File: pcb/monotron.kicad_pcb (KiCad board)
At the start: 2 copper layers, 133.3 x 94 mm, 51 parts, among them J1 Mono / Stereo, J10 DIN5-180, J11 DIN5-180, J12 DE9M, J13 DB25_Female, J14 Mini-DIN-6, J15 Mini-DIN-6, J2 Jack-DC, J3 1x7 Header, J4 AudioJack3, J5 DE9F, J6 1x4 Header, J7 DE15HD, J8 2x6 Header, J9 DIN5-180, U1 TM4C123G_Launchpad, U2 MAX3232, U3 74LS14, U4 6N138, U5 ATmega48A-PU

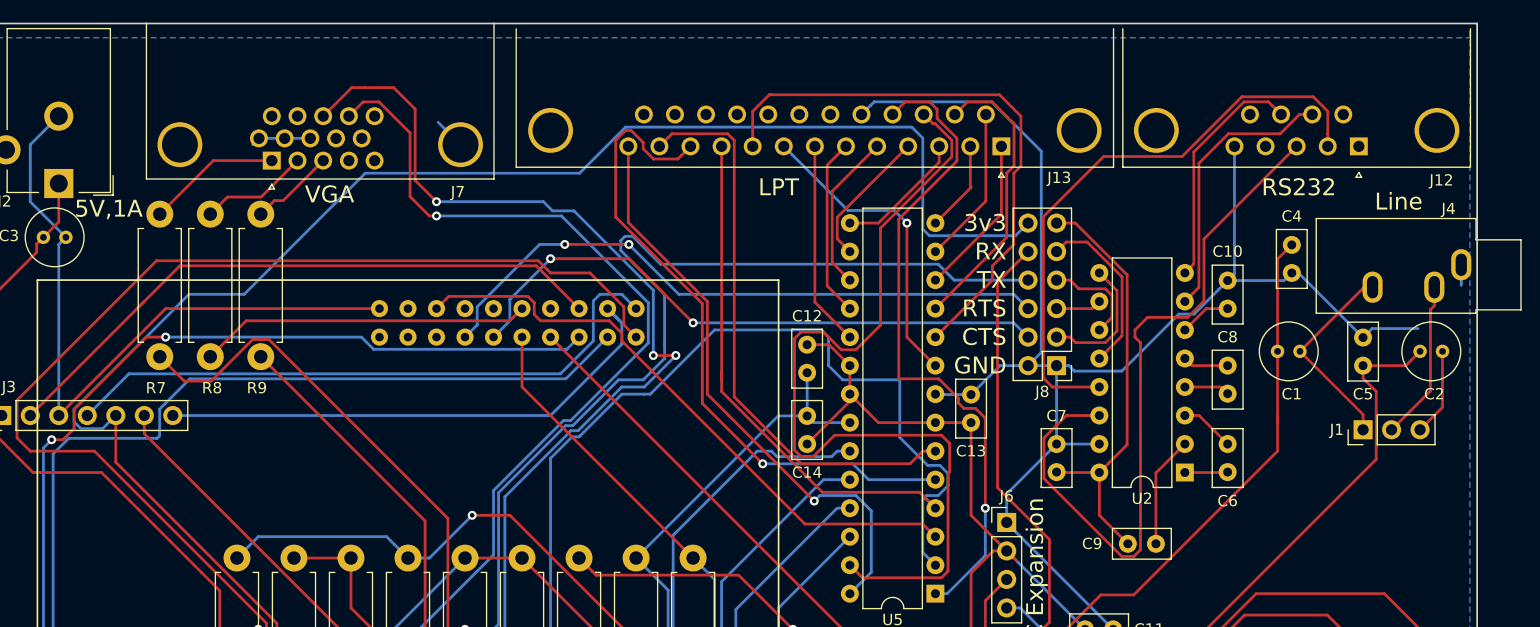
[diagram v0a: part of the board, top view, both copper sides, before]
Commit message: Fix split ground-plane. Moved a few bottom tracks to make ground fill larger.
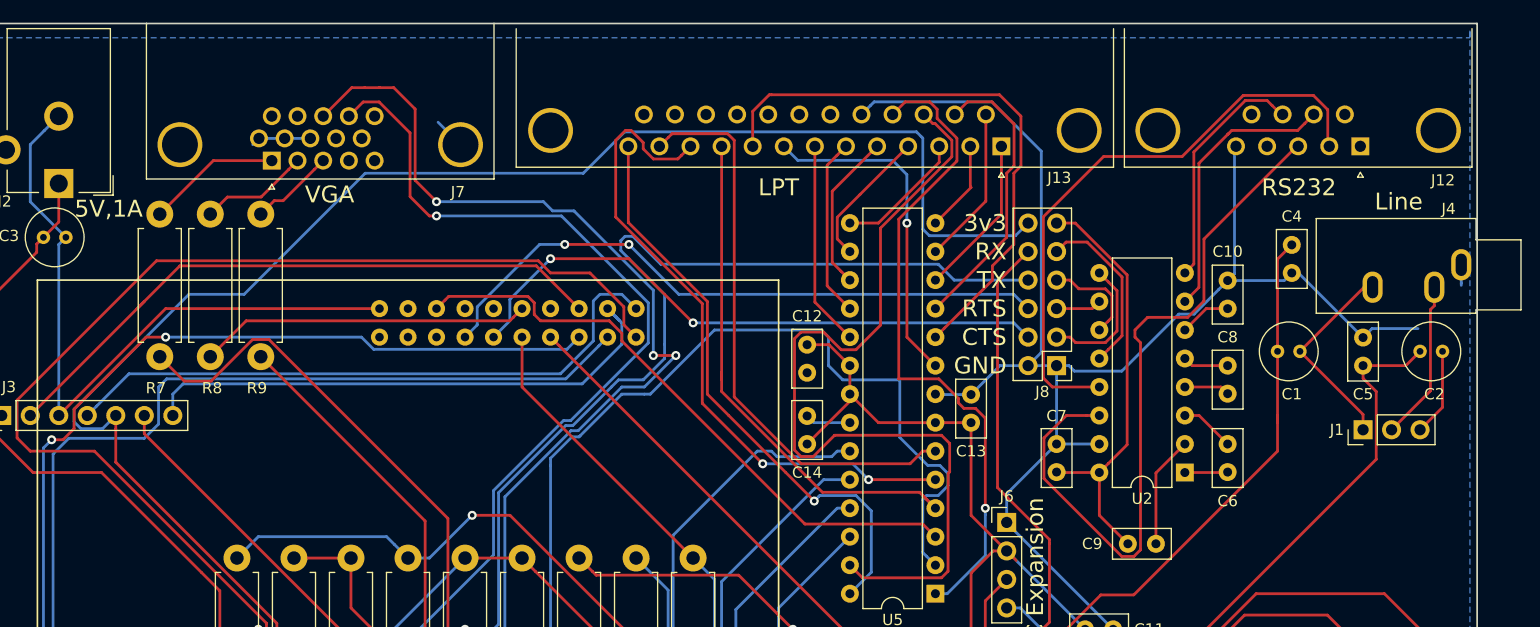
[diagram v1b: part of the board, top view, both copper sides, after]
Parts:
- moved J12 0.14 mm to (196.6, 46.5)
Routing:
- net GND: track 400.8 -> 376.5 mm
- net /Monotron I/O Expansion/D6: track 27.6 -> 30.1 mm
- net /PA3_SD_CS: track 47.9 -> 49.0 mm
- net /Monotron I/O Expansion/BUSY: vias 1 -> 2

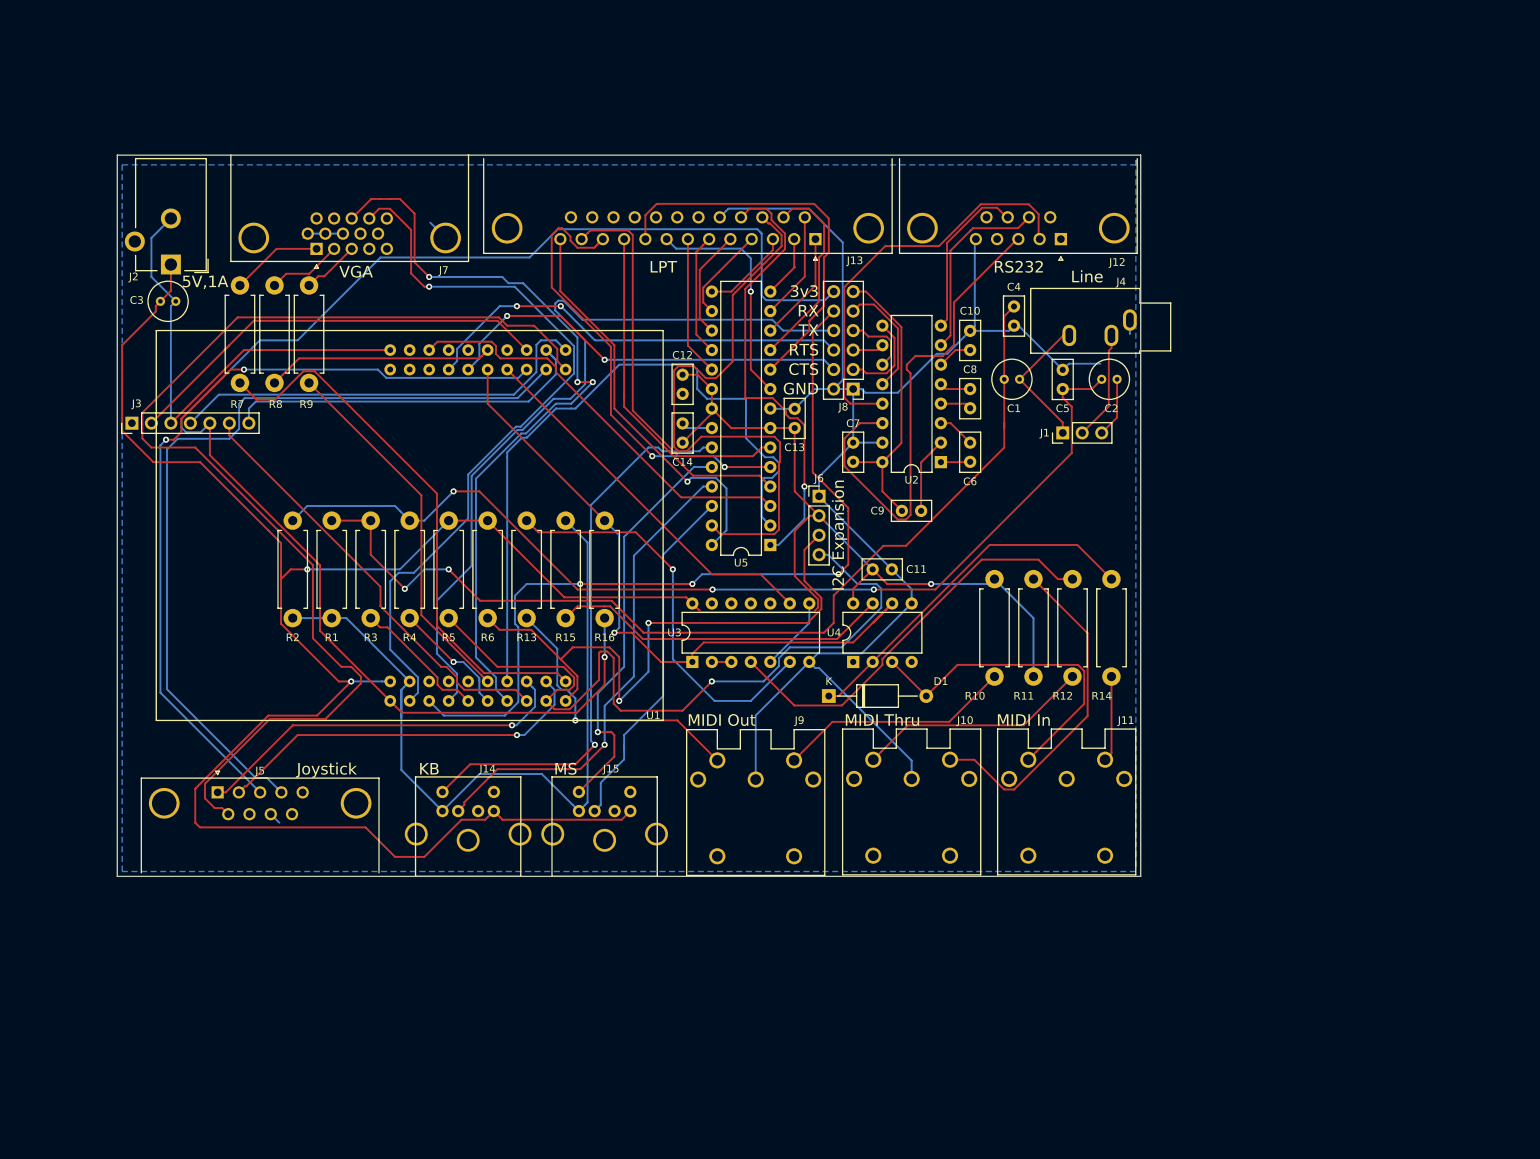
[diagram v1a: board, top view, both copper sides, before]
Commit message: Finished adding RTC to PCB layout.
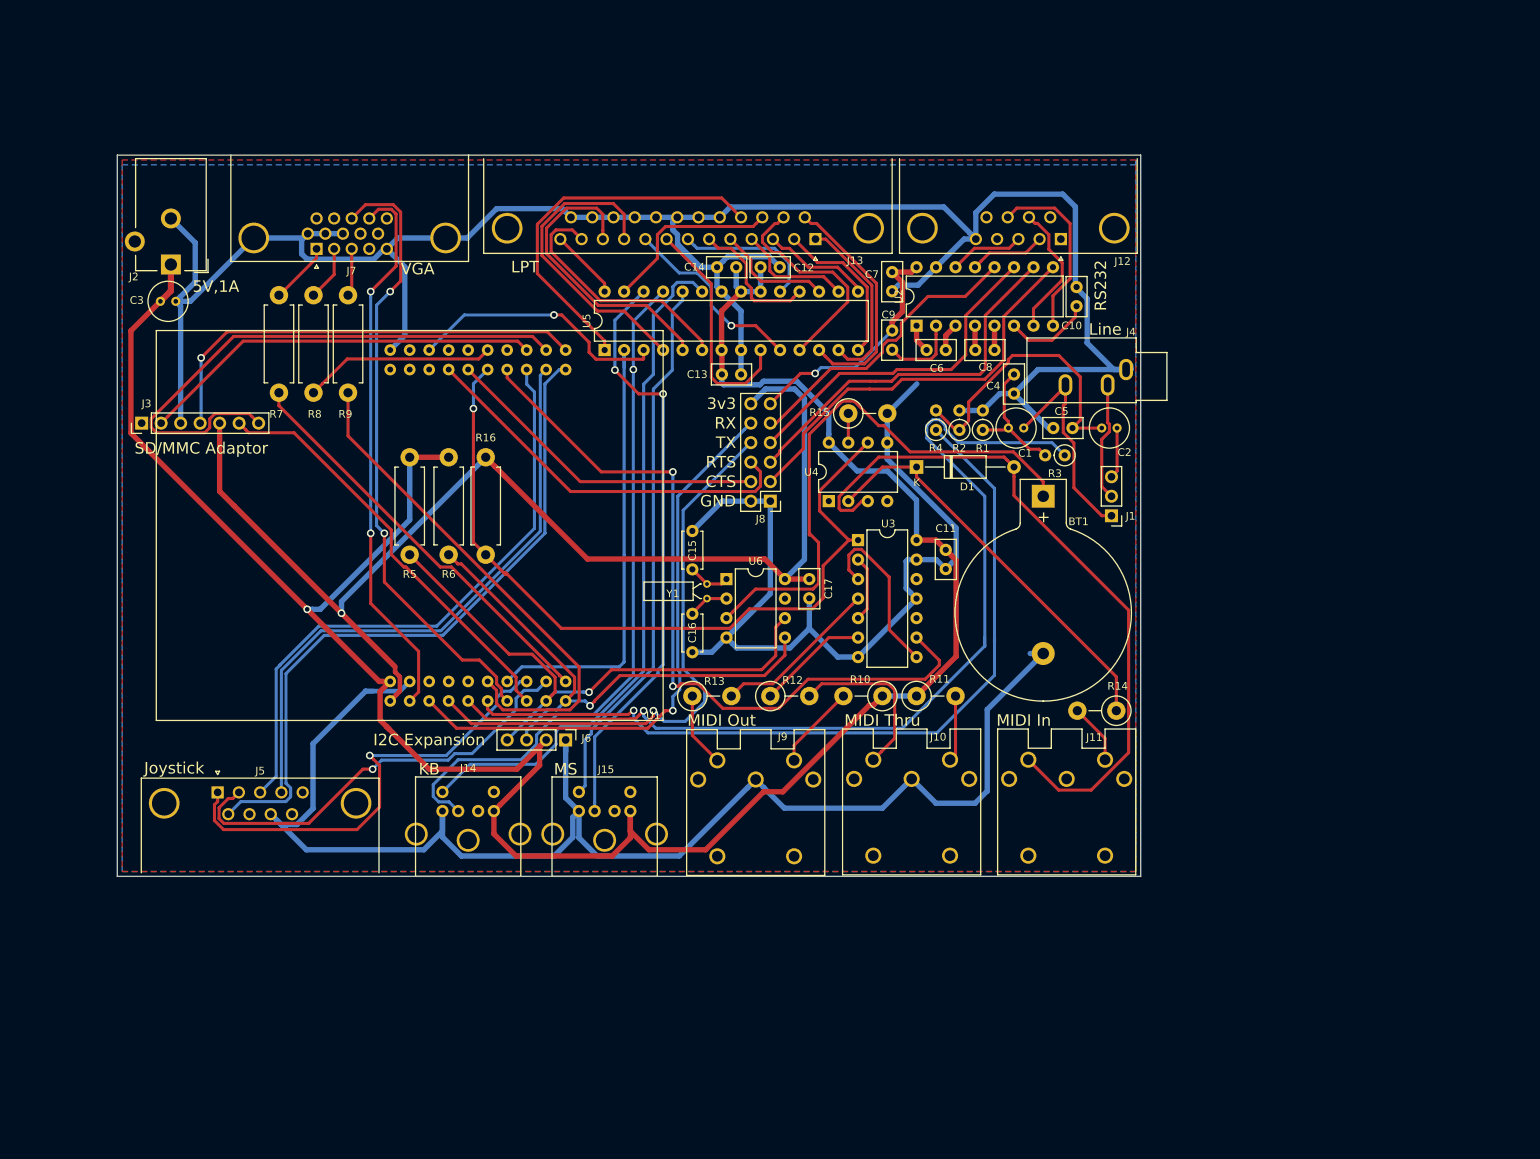
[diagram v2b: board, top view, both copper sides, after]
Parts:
- added BT1: Battery, Battery:BatteryHolder_Keystone_103_1x20mm, F.Cu at (194.3, 80.0)
- added C15: 12p, Capacitor_THT:C_Disc_D4.7mm_W2.5mm_P5.00mm, F.Cu at (148.6, 84.5)
- added C16: 12p, Capacitor_THT:C_Disc_D4.7mm_W2.5mm_P5.00mm, F.Cu at (148.6, 100.3)
- added C17: 100n, Capacitor_THT:C_Disc_D5.0mm_W2.5mm_P2.50mm, F.Cu at (163.8, 90.8)
- added U6: MCP7940N-xP, Package_DIP:DIP-8_W7.62mm, F.Cu at (153.0, 90.8)
- added Y1: 32,768 kHz, Crystal:Crystal_DS26_D2.0mm_L6.0mm_Horizontal, F.Cu at (150.5, 91.4)
- R1, R2, R3, R4: footprint Resistor_THT:R_Axial_DIN0411_L9.9mm_D3.6mm_P12.70mm_Horizontal -> Resistor_THT:R_Axial_DIN0207_L6.3mm_D2.5mm_P2.54mm_Vertical
- R10, R11, R12, R13, R14, R15: footprint Resistor_THT:R_Axial_DIN0411_L9.9mm_D3.6mm_P12.70mm_Horizontal -> Resistor_THT:R_Axial_DIN0411_L9.9mm_D3.6mm_P5.08mm_Vertical
- moved R3 92.9 mm to (197.1, 74.7), turned to 180 degrees
- moved R2 87.7 mm to (183.4, 71.4), turned to 90 degrees
- moved R1 85.7 mm to (186.4, 71.4), turned to 90 degrees
- moved R4 72.8 mm to (180.3, 71.4)
- moved J6 45.8 mm to (132.1, 111.8), turned to 270 degrees
- moved R15 45.5 mm to (168.9, 69.2), turned to 0 degrees
- moved R12 42.2 mm to (158.8, 106.0), turned to 0 degrees
- moved U5 33.3 mm to (137.2, 61.0), turned to 90 degrees
- moved D1 32.0 mm to (177.8, 76.2)
- moved U3 26.8 mm to (170.2, 85.7), turned to 0 degrees
- moved R16 26.1 mm to (121.7, 74.9), turned to 270 degrees
- moved C7 25.2 mm to (174.6, 50.8), turned to 270 degrees
- moved C14 23.9 mm to (154.3, 50.2), turned to 180 degrees
- moved R13 23.9 mm to (148.6, 106.0), turned to 0 degrees
- moved C9 23.5 mm to (174.6, 58.4), turned to 270 degrees
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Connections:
- U3 pad 3: Net-(U3-Pad2) -> Net-(U3-Pad3)
- U3 pad 4: Net-(R12-Pad1) -> Net-(R13-Pad2)
- U3 pad 5: Net-(U3-Pad5) -> Net-(U3-Pad2)
- U3 pad 6: Net-(R13-Pad2) -> Net-(R12-Pad1)
- U3 pad 8: Net-(U3-Pad5) -> Net-(U3-Pad3)
- U5 pad 12: /Monotron I/O Expansion/STROBE -> /Monotron I/O Expansion/AUTOF
- U5 pad 13: /Monotron I/O Expansion/AUTOF -> /Monotron I/O Expansion/STROBE
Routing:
- net GND: track 376.5 -> 588.6 mm
- net Net-(C1-Pad1): track 130.0 -> 17.4 mm, vias 2 -> 0
- net /PE4_AUDIO_L: track 17.7 -> 128.0 mm, vias 0 -> 1
- net Net-(C2-Pad1): track 131.8 -> 37.6 mm, vias 3 -> 0
- net /PE5_AUDIO_R: track 15.7 -> 108.3 mm
- net +BATT: track 0.00 -> 72.6 mm
- net /PF4_JS_FIRE: track 146.7 -> 89.6 mm
- net /RS232_TX: track 65.3 -> 9.71 mm
- net /Monotron I/O Expansion/INIT: track 78.0 -> 23.8 mm
- net /PC7_MIDI_OUT: track 49.5 -> 99.0 mm, vias 0 -> 2
- net Net-(D1-Pad2): track 43.5 -> 91.5 mm
- net /DTE_RTS: track 4.07 -> 49.1 mm
- net /RS232_RX: track 53.3 -> 9.94 mm
- net /Monotron I/O Expansion/SEL: track 52.5 -> 9.23 mm, vias 1 -> 0
- net +5V: track 352.9 -> 310.2 mm, vias 3 -> 1
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- added copper zone on F.Cu, net GND
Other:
- net class Default: trace_width 0.25 -> 0.4; via_dia 0.8 -> 1; via_drill 0.4 -> 0.6
- rule trace_min: 0.2 -> 0.1524
- board text added: "SD/MMC Adaptor"

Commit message: Cleaned up PCB layout a bit.
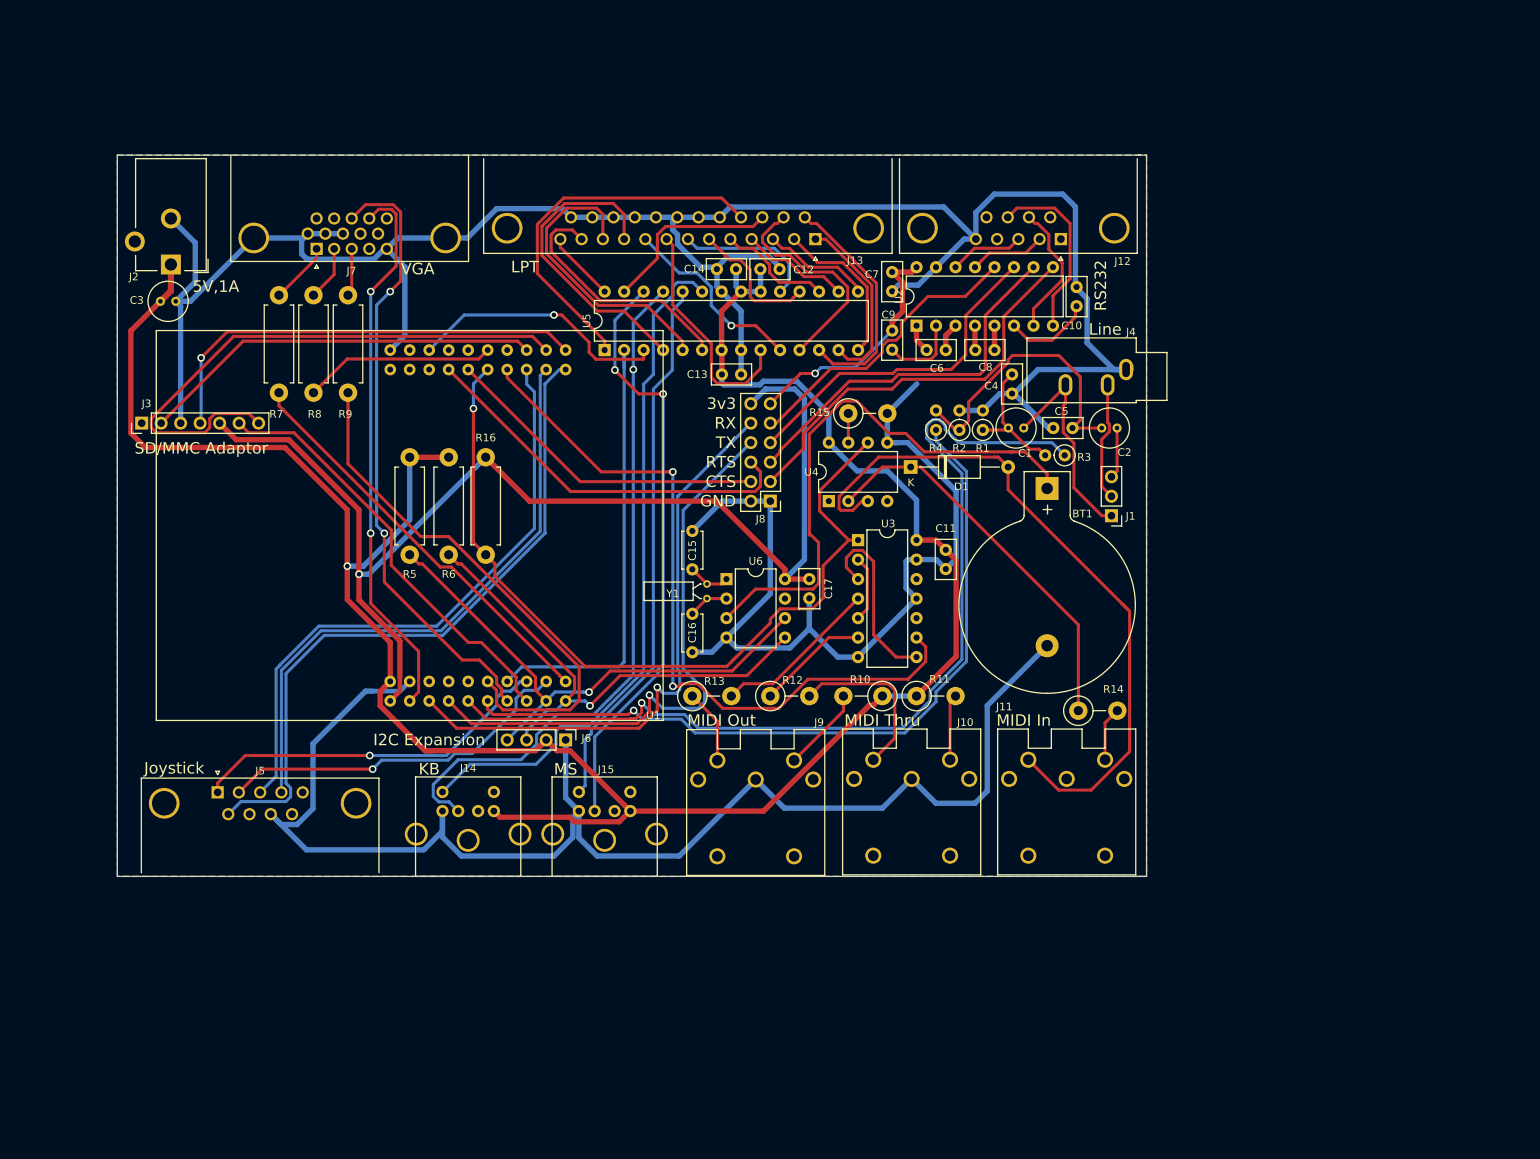
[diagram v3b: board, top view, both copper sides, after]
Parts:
- moved R14 4.95 mm to (198.9, 108.0), turned to 0 degrees
- moved BT1 1.14 mm to (194.8, 79.0)
- moved D1 0.76 mm to (177.0, 76.2)
- moved C14 0.26 mm to (154.3, 50.4)
- moved C12 0.26 mm to (157.5, 50.4)
- moved C4 0.25 mm to (190.2, 64.1)
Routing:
- net /PE2_JS_UP: track 59.4 -> 47.6 mm
- net +5V: track 310.2 -> 299.7 mm
- net /PE3_JS_DOWN: track 56.2 -> 46.9 mm
- net /PE5_AUDIO_R: track 108.3 -> 101.5 mm
- net /PC6_MIDI_IN: track 102.5 -> 109.1 mm
- net /PA6_I2C_SCL: track 74.1 -> 69.5 mm
- net /PC7_MIDI_OUT: track 99.0 -> 96.2 mm
- net /PD3_VGA_BLU: track 67.6 -> 69.7 mm
- net Net-(D1-Pad1): track 53.3 -> 51.5 mm
- net Net-(U3-Pad3): track 22.6 -> 24.3 mm
- net /PE4_AUDIO_L: track 128.0 -> 126.3 mm
- net /PA7_I2C_SDA: track 68.4 -> 67.0 mm
- net /PB0_U1RX: track 76.1 -> 77.4 mm
- net /PB1_U1TX: track 75.9 -> 77.0 mm
- net GND: track 588.6 -> 589.7 mm
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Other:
- board size 133.3 x 94 mm -> 134.1 x 94 mm
